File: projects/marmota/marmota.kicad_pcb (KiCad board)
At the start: 2 copper layers, 70 x 70 mm, 66 parts, among them J1 USB_C, J2 Conn_01x20_Pin, J3 Conn_01x20_Pin, SW1 Button top, SW2 Button side, U1 RP2040, U2 FLASH, U3 MCP73871, U4 RT6150B, U5 ESP32, Y1 12MHz

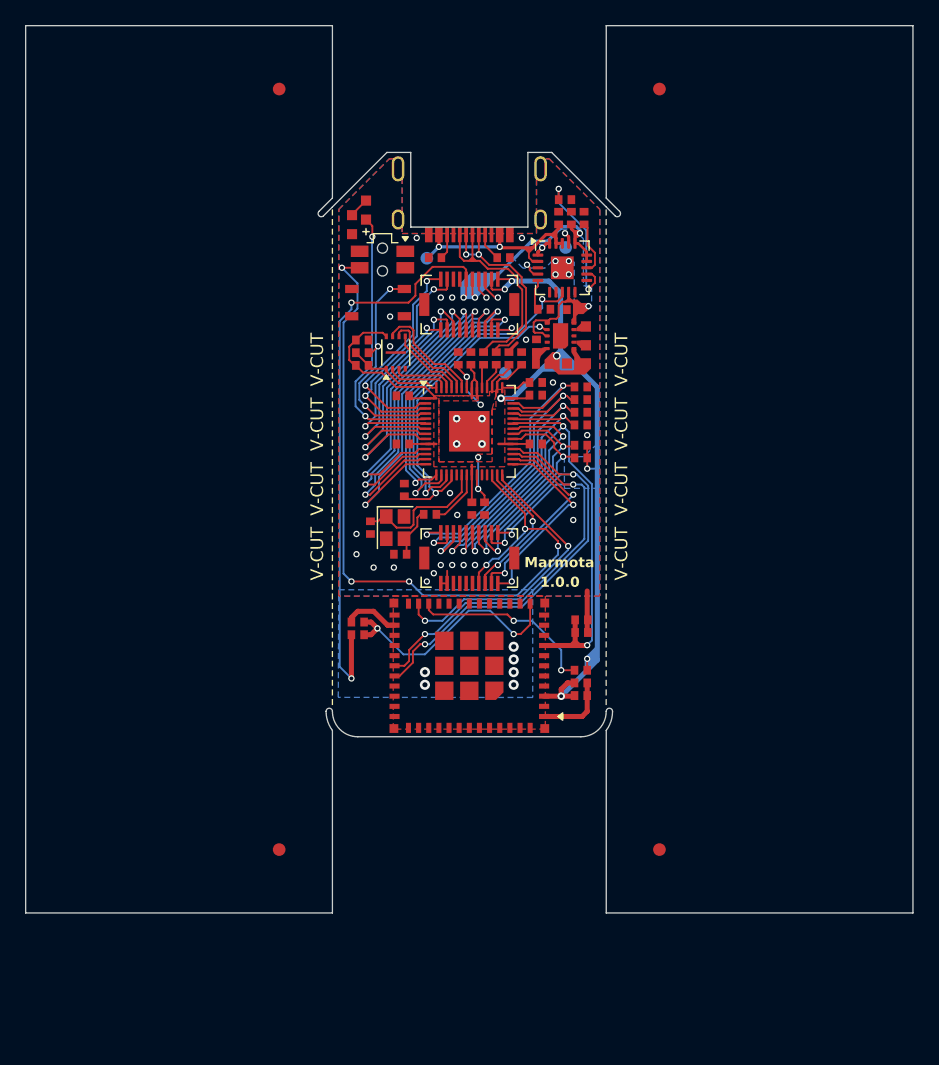
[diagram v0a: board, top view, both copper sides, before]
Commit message: Better Marmota v-cut indications
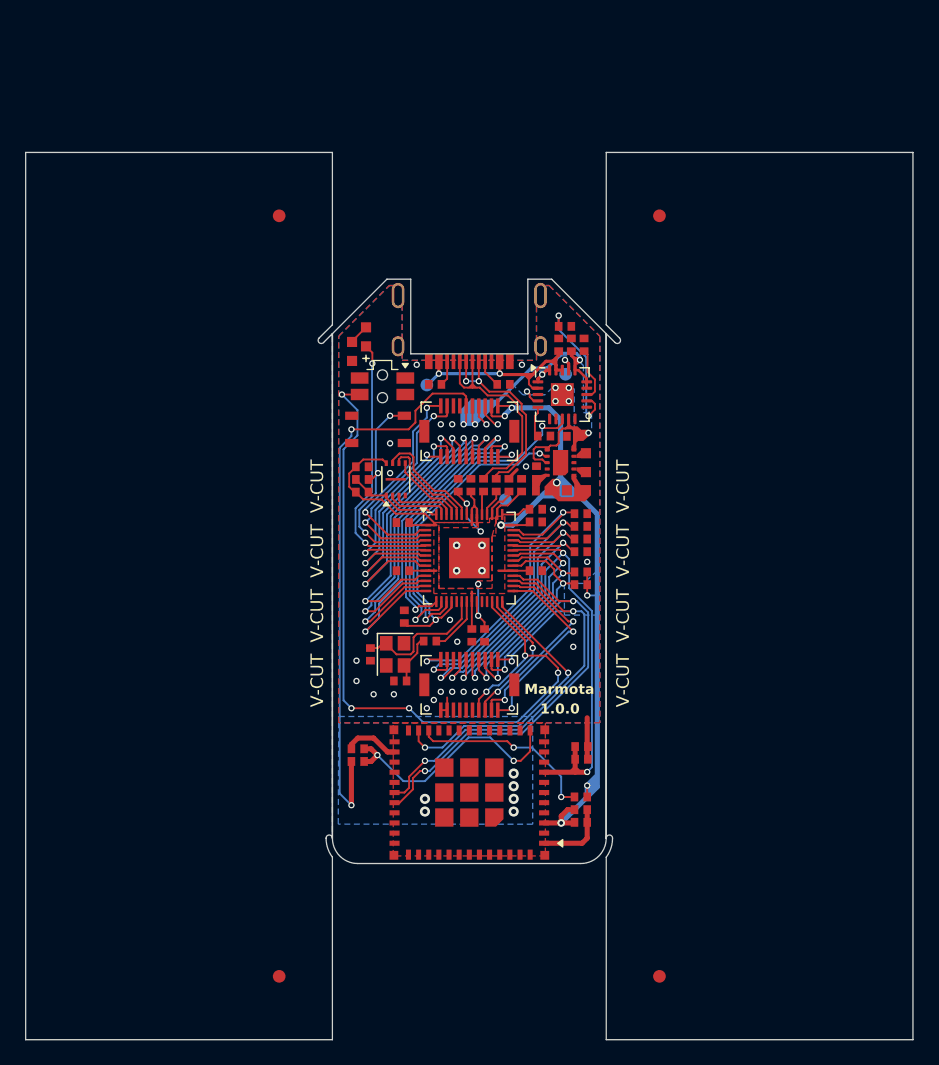
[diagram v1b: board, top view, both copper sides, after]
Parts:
- moved ? 10.0 mm to (67.1, 84.6)
- moved C10 10.0 mm to (64.1, 56.2)
- moved C11 10.0 mm to (54.8, 59.2)
- moved C12 10.0 mm to (65.2, 63.0)
- moved C13 10.0 mm to (54.8, 63.0)
- moved C15 10.0 mm to (65.2, 59.1)
- moved C16 10.0 mm to (65.2, 58.1)
- moved C20 10.0 mm to (51.5, 54.8)
- moved C3 10.0 mm to (54.5, 71.7)
- moved C30 10.0 mm to (67.0, 45.2)
- moved C32 10.0 mm to (68.0, 45.2)
- moved C41 10.0 mm to (68.2, 52.4)
- moved C42 10.0 mm to (68.5, 56.6)
- moved C50 10.0 mm to (68.8, 81.8)
- moved C51 10.0 mm to (68.8, 82.8)
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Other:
- board text added: "V-CUT"

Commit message: Fixed Marmota schematic parity
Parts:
- renumbered R54 to R50
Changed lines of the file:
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@@
 		(layer "F.Cu")
 		(at 68.85 76.875)
-		(property "Reference" "R54"
+		(property "Reference" "R50"
 			(at 0 0 90)
 			(layer "Cmts.User")

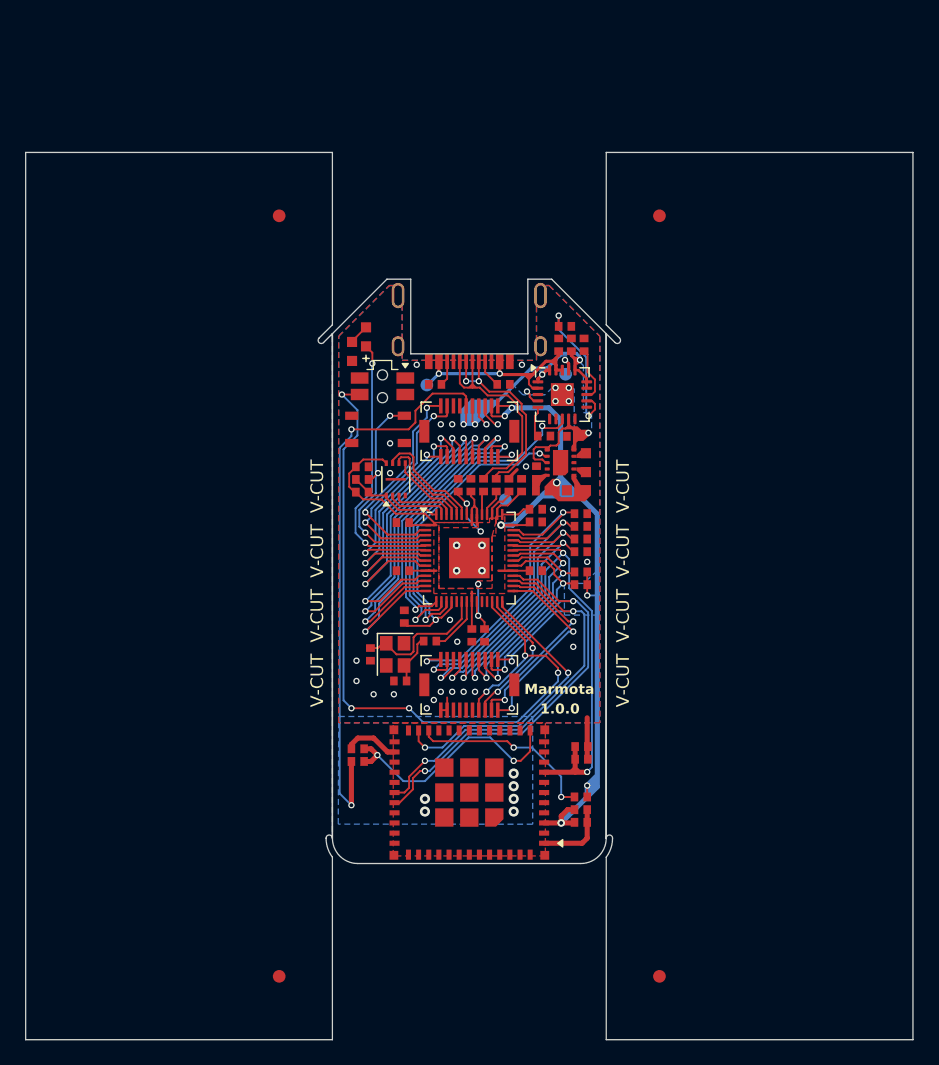
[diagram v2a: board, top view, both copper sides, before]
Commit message: Initial schematic for nRF52840+nPM1300
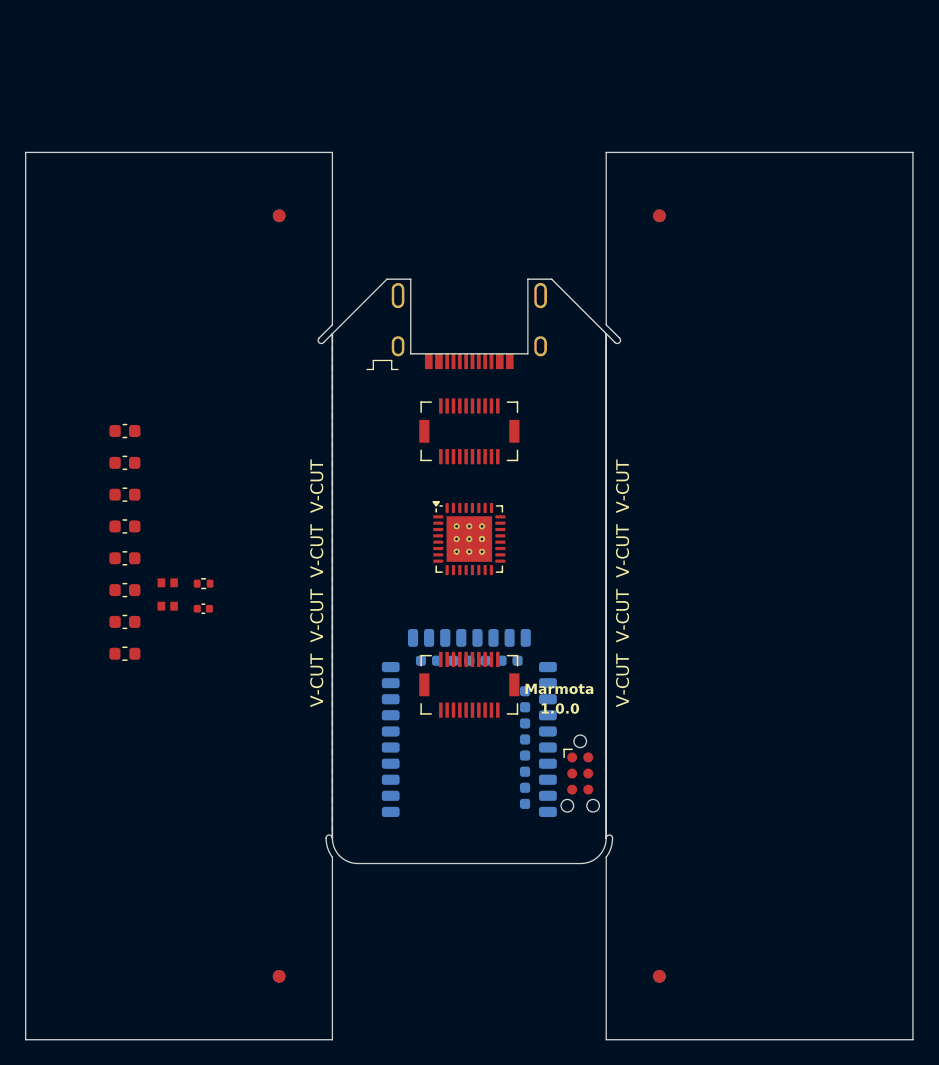
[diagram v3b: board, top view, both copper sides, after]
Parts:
- removed ?: , clipboard:5e7cfdf6-62b4-49b8-8e4d-08e3e4b200c4
- removed C13, C14, C15, C16, C20, C50, C61, C62, C63, C64: 100nF, ILO_fp:0402_compact
- removed C2, C3: 15pF, ILO_fp:0402_compact
- removed C30, C41, C51: 10uF, ILO_fp:0402_compact
- removed C32: 4.7uF, ILO_fp:0402_compact
- removed C42: 47uF, ILO_fp:0603_compact
- removed C52: 1uF, ILO_fp:0402_compact
- removed D1: Diode, ILO_fp:0603_d
- removed G*** (x2): LOGO, LOGO
- removed R20: 1KΩ, ILO_fp:0402_compact
- removed R21, R33, R34, R51, R52, R53: 10KΩ, ILO_fp:0402_compact
- removed R3, R4: 27Ω, ILO_fp:0402_compact
- removed R32: 3.3KΩ, ILO_fp:0402_compact
- removed R35: 487KΩ, ILO_fp:0402_compact
- removed R36, R37, R50: 86.6KΩ, ILO_fp:0402_compact
- removed R6: 20Ω, ILO_fp:0603
- removed R7, R8: 4.7KΩ, ILO_fp:0402_compact
- removed REF** (x5): Pad_1mm, ILO_fp:Pad_1mm
- removed SW1: Button top, ILO_fp:Alpsalpine_SKRP_compact
- removed SW2: Button side, ILO_fp:Alpsalpine_SKSC
- removed U1: RP2040, Package_DFN_QFN:QFN-56-1EP_7x7mm_P0.4mm_EP3.2x3.2mm
- removed U2: FLASH, ILO_fp:Winbond_W25Q
- removed U3: MCP73871, ILO_fp:QFN20_internal_routing
- removed U4: RT6150B, ILO_fp:WDFN-10L-2.5x2.5
- removed U5: ESP32, ILO_fp:Espressif_ESP32_mini
- removed Y1: 12MHz, Crystal:Crystal_SMD_2520-4Pin_2.5x2.0mm
- added C5: 100nF, Capacitor_SMD:C_0402_1005Metric, F.Cu at (39.0, 66.0)
- added J4: TC2030-NL, Connector:Tag-Connect_TC2030-IDC-NL_2x03_P1.27mm_Vertical, F.Cu at (68.8, 79.0)
- added U6: nRF52840_E73-2G4M08S1C, PCM_marbastlib-various:nRF52840_E73-2G4M08S1C, B.Cu at (60.0, 77.0)
- added U7: nPM1300-QEXX, Package_DFN_QFN:QFN-32-1EP_5x5mm_P0.5mm_EP3.6x3.6mm_ThermalVias, F.Cu at (60.0, 60.5)
- C10: footprint ILO_fp:0402_compact -> Capacitor_SMD:C_0603_1608Metric
- C11, C6, C7: value 100nF -> 10uF; footprint ILO_fp:0402_compact -> Capacitor_SMD:C_0603_1608Metric
- C12: value 100nF -> 2.2uF; footprint ILO_fp:0402_compact -> Capacitor_SMD:C_0603_1608Metric
- C8: value 1uF -> 10uF; footprint ILO_fp:0402_compact -> Capacitor_SMD:C_0603_1608Metric
- C9: value 100nF -> 1uF; footprint ILO_fp:0402_compact -> Capacitor_SMD:C_0603_1608Metric
- L1: footprint ILO_fp:0603_compact -> Inductor_SMD:L_0603_1608Metric
- R5: value 1KΩ -> 330kR; footprint ILO_fp:0402_compact -> Resistor_SMD:R_0402_1005Metric
- moved L1 39.4 mm to (32.8, 69.5), turned to 0 degrees
- moved C12 32.7 mm to (32.8, 67.0), turned to 0 degrees
- moved C10 31.8 mm to (32.8, 62.0), turned to 0 degrees
- moved C7 31.5 mm to (32.8, 54.5), turned to 0 degrees
- moved R40 30.8 mm to (36.2, 64.0)
- moved C8 30.3 mm to (32.8, 57.0), turned to 0 degrees
- moved C9 27.5 mm to (32.8, 59.5), turned to 0 degrees
- moved R41 27.4 mm to (36.2, 65.8)
- moved C6 26.6 mm to (32.8, 52.0), turned to 0 degrees
- moved C11 22.6 mm to (32.8, 64.5)
- moved R5 18.4 mm to (39.0, 64.0), turned to 0 degrees
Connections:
- net /UBS_D+ renamed /USB_D+
- net /UBS_D- renamed /USB_D-
- C10 pad 1: GND -> VBUS
- C10 pad 2: +3V3 -> GND
- C11 pad 1: GND -> VDD
- C11 pad 2: +3V3 -> GND
- C12 pad 1: GND -> /BAT+
- C12 pad 2: +3V3 -> GND
- C6 pad 1: GND -> VSYS
- C6 pad 2: +1V1 -> GND
- C7 pad 1: GND -> VSYS
- C7 pad 2: +1V1 -> GND
- C8 pad 1: GND -> VSYS
- C8 pad 2: +1V1 -> GND
- C9 pad 1: GND -> Net-(U7-VBUS)
- C9 pad 2: +3V3 -> GND
- J1 pad A4: VBUS -> Net-(U7-VBUS)
- J1 pad A9: VBUS -> Net-(U7-VBUS)
- J1 pad B4: VBUS -> Net-(U7-VBUS)
- J1 pad B9: VBUS -> Net-(U7-VBUS)
- J2 pad 10: +3V3 -> VDD
- J2 pad 9: +3V3 -> VDD
- L1 pad 1: Net-(U4-LX2) -> VDD
- R5 pad 1: /XOUT -> Net-(U7-VSET2)
- R5 pad 2: Net-(C3-Pad1) -> GND
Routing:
- net +3V3: track 90.6 -> 0.00 mm, vias 7 -> 0
- net /BAT+: track 64.0 -> 0.00 mm, vias 5 -> 0
- net /RUN: track 60.9 -> 0.00 mm, vias 6 -> 0
- net /GP25: track 43.5 -> 0.00 mm, vias 3 -> 0
- net /UART1_RX: track 41.7 -> 0.00 mm, vias 3 -> 0
- net /UART1_TX: track 38.3 -> 0.00 mm, vias 3 -> 0
- net /GP11: track 28.3 -> 0.00 mm, vias 2 -> 0
- net /GP10: track 26.4 -> 0.00 mm, vias 2 -> 0
- net /GP14: track 26.3 -> 0.00 mm, vias 2 -> 0
- net /GP15: track 25.7 -> 0.00 mm, vias 2 -> 0
- net /ADC3: track 24.6 -> 0.00 mm, vias 2 -> 0
- net /GP9: track 24.6 -> 0.00 mm, vias 2 -> 0
- net /ADC2: track 24.4 -> 0.00 mm, vias 2 -> 0
- net /GP17: track 23.6 -> 0.00 mm, vias 2 -> 0
- net /ADC1: track 23.4 -> 0.00 mm, vias 2 -> 0
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- removed copper zone on F.Cu, net +1V1
- removed copper zone on B.Cu, net +3V3
- removed copper zone on F.Cu, net +3V3
- removed copper zone on B.Cu, net GND
- removed copper zone on F.Cu, net GND
- removed copper zone on B.Cu, net VSYS
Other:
- board text removed: "3V3"
- board text removed: "BAT"
- board text removed: "GND"
- board text removed: "VBUS"
- board text removed: "VSYS"

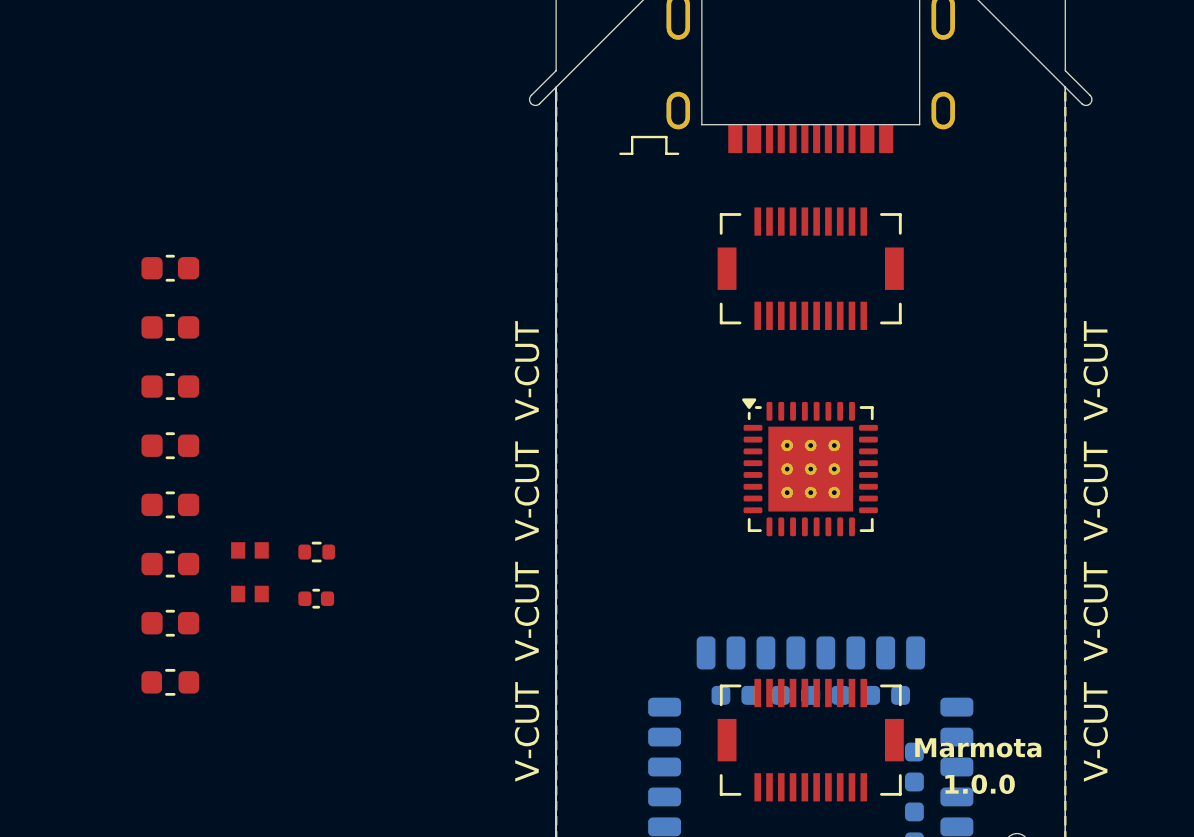
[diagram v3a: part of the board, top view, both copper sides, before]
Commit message: Reworked Alpakka w/ interrupt lines, etc
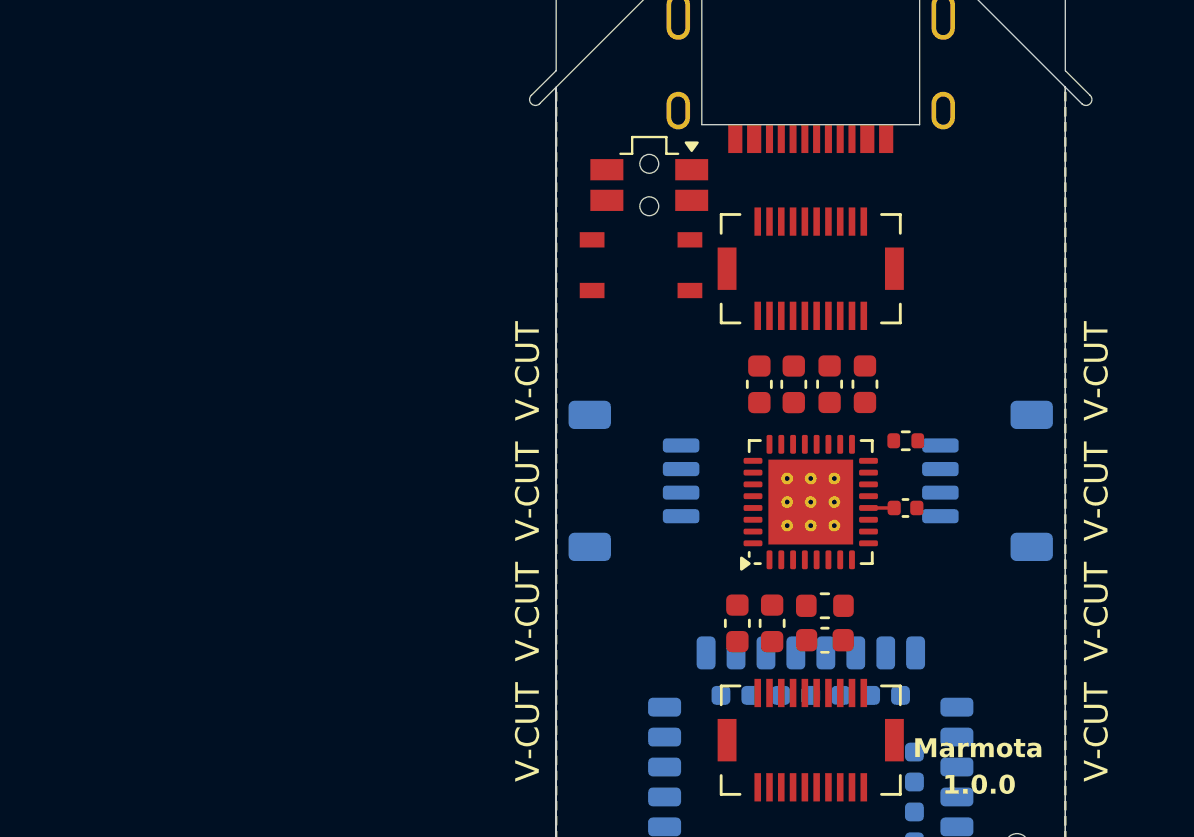
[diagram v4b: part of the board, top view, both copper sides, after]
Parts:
- removed R40, R41: 5.1KΩ, ILO_fp:0402_compact
- added J5: Conn_01x04_MountingPin, Connector_JST:JST_SH_SM04B-SRSS-TB_1x04-1MP_P1.00mm_Horizontal, B.Cu at (67.5, 61.0)
- added J6: Conn_01x04_MountingPin, Connector_JST:JST_SH_SM04B-SRSS-TB_1x04-1MP_P1.00mm_Horizontal, B.Cu at (52.5, 61.0)
- added SW1: Button top, ILO_fp:Alpsalpine_SKRP_compact, F.Cu at (52.8, 51.9)
- added SW2: Button side, ILO_fp:Alpsalpine_SKSC, F.Cu at (53.1, 48.5)
- moved C12 31.2 mm to (62.3, 56.9), turned to 90 degrees
- moved C7 28.5 mm to (58.4, 67.0), turned to -90 degrees
- moved C6 28.4 mm to (60.8, 56.9), turned to 90 degrees
- moved L1 28.0 mm to (60.6, 66.3)
- moved C11 28.0 mm to (60.6, 67.8)
- moved C9 26.6 mm to (59.3, 56.9), turned to 90 degrees
- moved C8 26.1 mm to (56.9, 67.0), turned to -90 degrees
- moved C10 25.5 mm to (57.8, 56.9), turned to 90 degrees
- moved R5 25.4 mm to (64.0, 59.3)
- moved C5 25.3 mm to (64.0, 62.1)
- moved U7 1.40 mm to (60.0, 61.9), turned to 90 degrees
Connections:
- J1 pad A5: Net-(J1-CC1) -> /USB.CC1
- J1 pad B5: Net-(J1-CC2) -> /USB.CC2
- U6 pad 11: unconnected-(U6-P0.00/XL1-Pad11) -> Net-(U6-P0.00/XL1)
- U6 pad 13: unconnected-(U6-P0.01/XL2-Pad13) -> Net-(U6-P0.01/XL2)
- U6 pad 9: unconnected-(U6-P0.31/AIN7-Pad9) -> /NPM1300.INT
- U7 pad 8: /ENABLE -> unconnected-(U7-GPIO1-Pad8)
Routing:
- net VDD: track 0.00 -> 1.09 mm
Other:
- copper layers 2 -> 4
